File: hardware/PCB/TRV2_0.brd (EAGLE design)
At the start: 46 x 70 mm, 51 parts, among them IC1 TMP112, IC2 IC2, IC4 CNY70, IC5 ATMEGA8-AU, Q1 FC-12M, U1 DRV8850_RGY_24

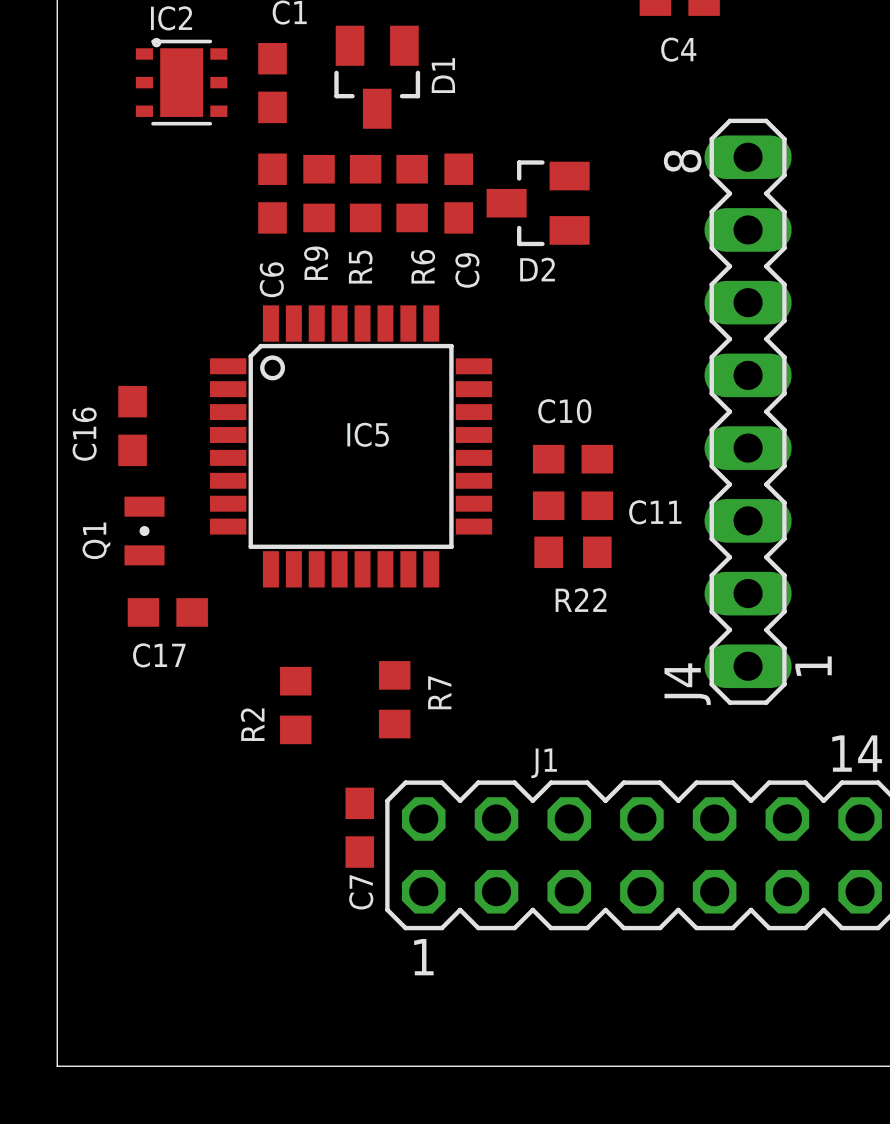
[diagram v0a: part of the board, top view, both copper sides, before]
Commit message: intial "core" tracks layed out
copy of tracks as per enlight
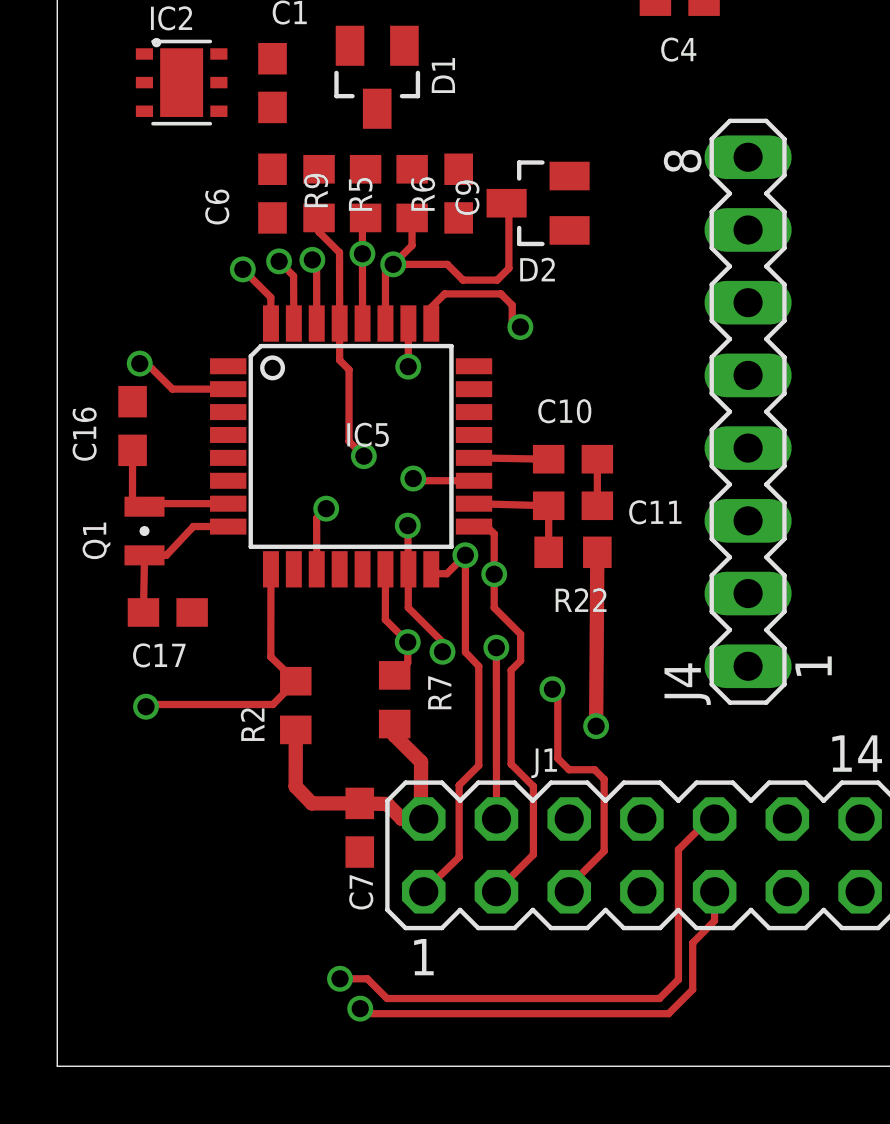
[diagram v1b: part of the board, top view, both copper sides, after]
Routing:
- net SDA: track 0.00 -> 29.5 mm, vias 0 -> 2
- net SCL: track 0.00 -> 19.5 mm, vias 0 -> 2
- net RESET: track 0.00 -> 17.8 mm, vias 0 -> 2
- net VCC: track 0.00 -> 16.7 mm, vias 0 -> 1
- net SPI_SCLK: track 0.00 -> 14.7 mm, vias 0 -> 1
- net SPI_MISO: track 0.00 -> 14.4 mm, vias 0 -> 1
- net SPI_MOSI: track 0.00 -> 10.9 mm, vias 0 -> 3
- net BUTTON_MODE_L: track 0.00 -> 9.88 mm, vias 0 -> 1
- net N$5: track 0.00 -> 5.35 mm
- net N$4: track 0.00 -> 5.23 mm
- net ML: track 0.00 -> 4.66 mm, vias 0 -> 1
- net AVCC: track 0.00 -> 4.23 mm
- net SPI_NNS: track 0.00 -> 4.22 mm, vias 0 -> 1
- net LED_HEATCALL_L: track 0.00 -> 3.46 mm, vias 0 -> 1
- net AREF: track 0.00 -> 2.61 mm
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
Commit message: Before routing tracks
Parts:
- moved J4 16.0 mm to (40.0, 21.0)
- moved C13 15.3 mm to (16.5, 47.0), turned to 180 degrees
- moved C12 12.3 mm to (16.5, 48.9), turned to 180 degrees
- moved C5 8.35 mm to (16.5, 45.1)
- moved J3 7.83 mm to (11.2, 52.6), turned to 180 degrees
- moved R3 7.24 mm to (10.8, 42.5), turned to 180 degrees
- moved R16 6.48 mm to (16.5, 43.2), turned to 180 degrees
- moved U1 1.80 mm to (11.4, 47.0)
- moved U$2 1.27 mm to (12.7, 70.5), flipped to the bottom
- turned R13 to 270 degrees
- turned VR1 to 270 degrees
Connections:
- net MC: now also IC5.22
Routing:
- net VCC: track 16.7 -> 210.5 mm, vias 1 -> 19
- net IO_POWER_UP: track 2.26 -> 124.3 mm, vias 1 -> 5
- net BUTTON_MODE_L: track 9.88 -> 89.9 mm, vias 1 -> 2
- net SDA: track 29.5 -> 91.0 mm, vias 2 -> 5
- net SCL: track 19.5 -> 80.5 mm, vias 2 -> 5
- net MI: track 2.15 -> 61.1 mm, vias 1 -> 6
- net DQ: track 2.30 -> 60.6 mm, vias 1 -> 2
- net TXD0: track 2.28 -> 56.3 mm, vias 1 -> 2
- net RXD0: track 2.38 -> 56.4 mm, vias 1 -> 2
- net LDR: track 0.00 -> 51.7 mm, vias 0 -> 4
- net POT: track 0.00 -> 49.6 mm, vias 0 -> 1
- net LED_HEATCALL_L: track 3.46 -> 52.0 mm, vias 1 -> 4
- net RFMIRQ: track 0.00 -> 45.5 mm, vias 0 -> 5
- net MR: track 1.51 -> 24.4 mm, vias 1 -> 2
- net SPI_SCLK: track 14.7 -> 35.7 mm, vias 1 -> 3
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- added copper zone on layer 1, net GND
- added copper zone on layer 16, net GND

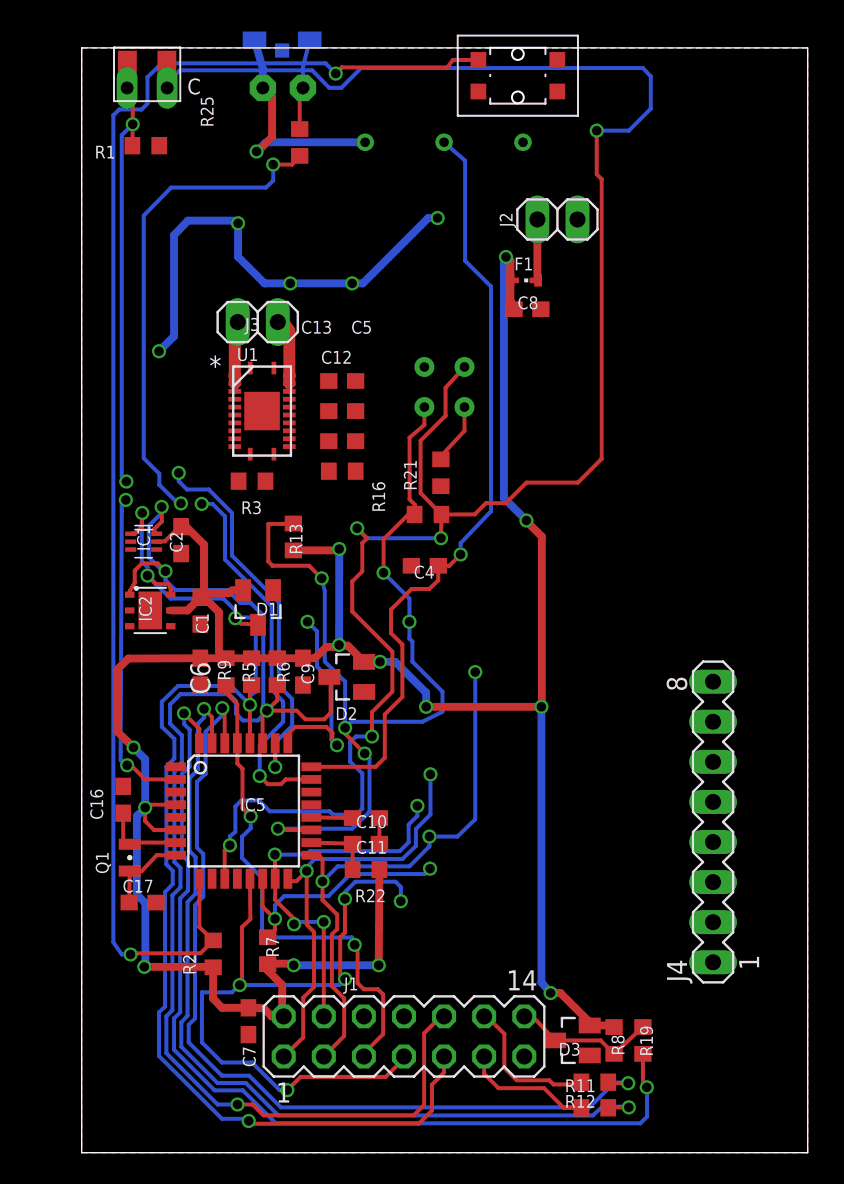
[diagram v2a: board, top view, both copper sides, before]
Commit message: 3 wires left
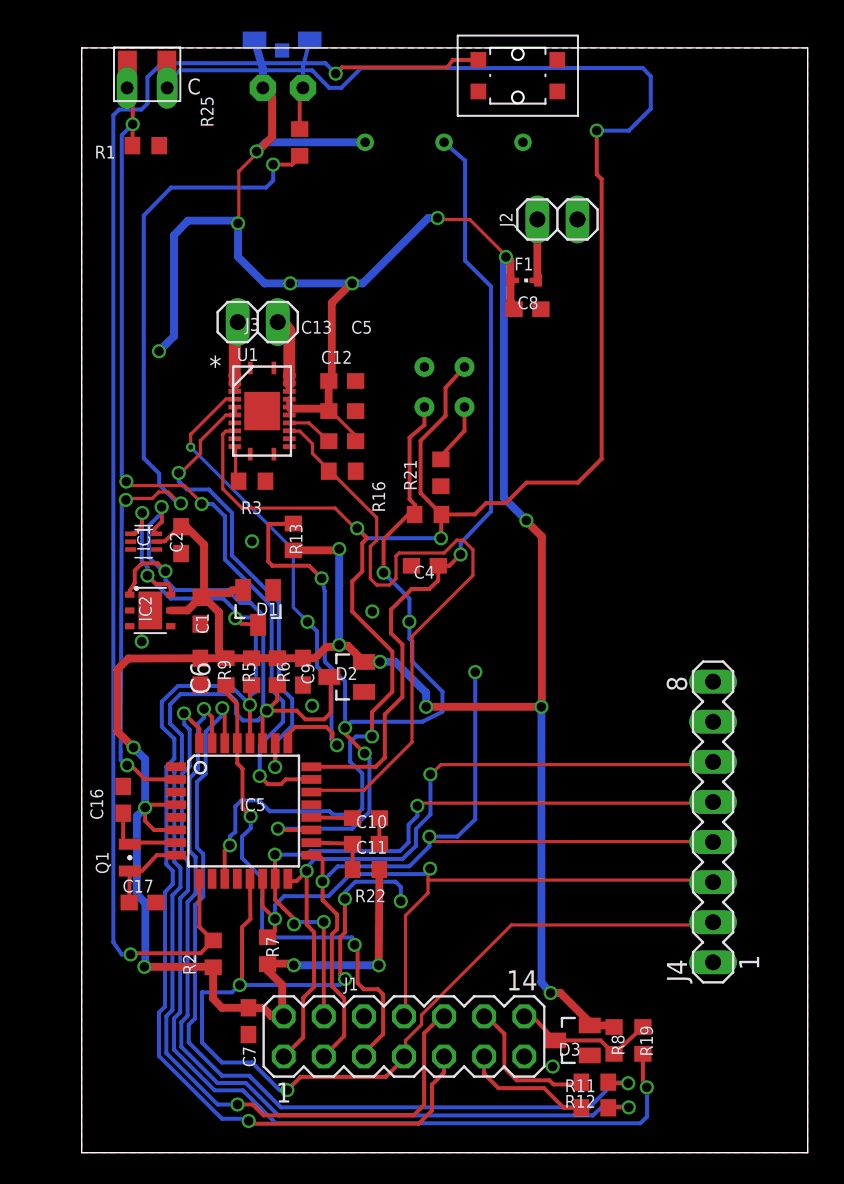
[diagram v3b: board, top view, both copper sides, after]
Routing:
- net MC: track 0.00 -> 42.7 mm
- net SPI_NNS: track 15.9 -> 44.0 mm
- net VCC: track 210.5 -> 236.0 mm
- net RFMIRQ: track 45.5 -> 69.6 mm
- net SPI_MOSI: track 24.2 -> 43.2 mm
- net ML: track 13.5 -> 32.4 mm, vias 2 -> 3
- net SPI_MISO: track 27.0 -> 45.2 mm
- net SPI_SCLK: track 35.7 -> 53.8 mm
- net IO_POWER_UP: track 124.3 -> 139.1 mm
- net MR: track 24.4 -> 30.5 mm
- net LDR: track 51.7 -> 57.1 mm
- net LED_HEATCALL_L: track 52.0 -> 56.0 mm
- net N$20: track 0.00 -> 2.95 mm
- net N$12: track 0.00 -> 2.32 mm
- net GND: vias 0 -> 5

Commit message: 2 wires left
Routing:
- net SPI_SCLK: track 53.8 -> 41.1 mm, vias 3 -> 2
- net GND: vias 5 -> 7
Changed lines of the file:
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@@
 <via x="3.81" y="32.385" extent="1-16" drill="0.6"/>
 <via x="10.795" y="38.735" extent="1-16" drill="0.6"/>
+<via x="25.4" y="32.385" extent="1-16" drill="0.6"/>
+<via x="17.78" y="28.067" extent="1-16" drill="0.6"/>
 <wire x1="6.2992" y1="37.9612" x2="4.75120625" y2="38.2176" width="0" layer="19" extent="1-1"/>
-<wire x1="17.8950125" y1="29.193196875" x2="14.605" y2="28.321" width="0" layer="19" extent="1-1"/>
 </signal>
 <signal name="SCL">
@@
 <wire x1="15.261809375" y1="16.012628125" x2="15.261809375" y2="17.184584375" width="0.254" layer="1"/>
 <via x="22.034925" y="20.030415625" extent="1-16" drill="0.6"/>
-<via x="24.93713125" y="30.4505125" extent="1-16" drill="0.6"/>
 <wire x1="22.034925" y1="20.030415625" x2="22.034925" y2="19.4093875" width="0.254" layer="16"/>
 <wire x1="22.034925" y1="19.4093875" x2="20.767975" y2="18.142434375" width="0.254" layer="16"/>
 <wire x1="20.767975" y1="18.142434375" x2="16.220103125" y2="18.142434375" width="0.254" layer="16"/>
 <wire x1="16.220103125" y1="18.142434375" x2="15.261809375" y2="17.184584375" width="0.254" layer="16"/>
-<wire x1="24.93713125" y1="30.4505125" x2="24.93713125" y2="21.12713125" width="0.254" layer="16"/>
-<wire x1="24.93713125" y1="21.12713125" x2="23.81013125" y2="20.030415625" width="0.254" layer="16"/>
-<wire x1="23.81013125" y1="20.030415625" x2="22.034925" y2="20.030415625" width="0.254" layer="16"/>
 <wire x1="22.352" y1="19.7104" x2="39.8272" y2="19.7104" width="0.2032" layer="1"/>
 <wire x1="22.1488" y1="19.9136" x2="22.352" y2="19.7104" width="0.2032" layer="1"/>

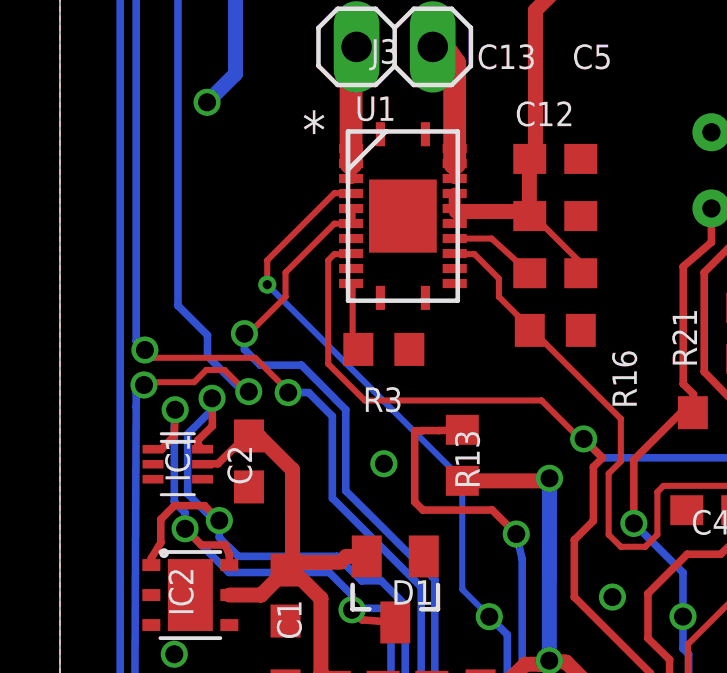
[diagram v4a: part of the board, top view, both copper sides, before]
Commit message: all wires done - need to do ERC and DRC
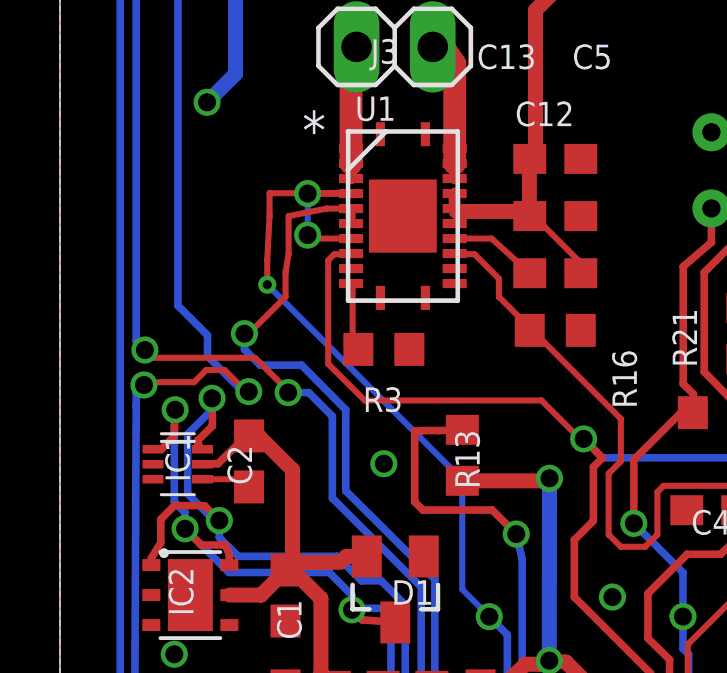
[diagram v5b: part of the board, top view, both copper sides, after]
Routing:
- net ML: track 32.4 -> 38.0 mm, vias 3 -> 5
- net GND: track 1.63 -> 3.43 mm
- net MR: track 30.5 -> 31.8 mm
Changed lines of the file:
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@@
 <via x="25.4" y="32.385" extent="1-16" drill="0.6"/>
 <via x="17.78" y="28.067" extent="1-16" drill="0.6"/>
-<wire x1="6.2992" y1="37.9612" x2="4.75120625" y2="38.2176" width="0" layer="19" extent="1-1"/>
+<wire x1="4.75120625" y1="38.2176" x2="6.2992" y2="38.2176" width="0.2032" layer="1"/>
+<wire x1="6.2992" y1="38.2176" x2="6.2992" y2="37.9612" width="0.4064" layer="1"/>
 </signal>
 <signal name="SCL">
@@
 <wire x1="16.174684375" y1="25.825634375" x2="16.174684375" y2="25.81956875" width="0.254" layer="16"/>
 <wire x1="9.7026" y1="47.74" x2="9.41" y2="47.74" width="0.254" layer="1"/>
-<wire x1="9.144" y1="47.752" x2="9.3472" y2="47.752" width="0.2032" layer="1"/>
-<wire x1="6.9088" y1="45.5168" x2="9.144" y2="47.752" width="0.2032" layer="1"/>
+<wire x1="6.9088" y1="45.5168" x2="6.985" y2="46.99" width="0.2032" layer="1"/>
+<wire x1="6.985" y1="46.99" x2="6.985" y2="47.752" width="0.2032" layer="1"/>
+<wire x1="6.985" y1="47.752" x2="9.3472" y2="47.752" width="0.2032" layer="1"/>
 <wire x1="6.9088" y1="44.704" x2="6.9088" y2="45.5168" width="0.2032" layer="1"/>
 <wire x1="13.4112" y1="38.2016" x2="6.9088" y2="44.704" width="0.2032" layer="16"/>
@@
 <wire x1="14.4272" y1="33.7312" x2="14.310025" y2="33.636434375" width="0.2032" layer="16"/>
 <via x="6.9088" y="44.704" extent="1-16" drill="0.3048"/>
-<wire x1="9.7026" y1="47.74" x2="9.7026" y2="46.24" width="0" layer="19" extent="1-1"/>
+<wire x1="9.7026" y1="46.24" x2="8.37" y2="46.24" width="0.2032" layer="1"/>
+<wire x1="9.7026" y1="47.74" x2="8.255" y2="47.74" width="0.2032" layer="1"/>
+<wire x1="8.255" y1="47.74" x2="8.255" y2="46.355" width="0.2032" layer="16"/>
+<via x="8.255" y="47.74" extent="1-16" drill="0.6"/>
+<via x="8.255" y="46.355" extent="1-16" drill="0.6"/>
+<wire x1="8.37" y1="46.24" x2="8.255" y2="46.355" width="0.2032" layer="1"/>
 </signal>
 <signal name="MR">
@@
 <wire x1="9.7536" y1="46.736" x2="9.7026" y2="46.74" width="0.2032" layer="1"/>
 <wire x1="9.7536" y1="47.1424" x2="9.7026" y2="47.24" width="0.2032" layer="1"/>
-<wire x1="9.144" y1="46.736" x2="9.5504" y2="46.736" width="0.2032" layer="1"/>
-<wire x1="7.5184" y1="45.1104" x2="9.144" y2="46.736" width="0.2032" layer="1"/>
+<wire x1="7.5184" y1="45.1104" x2="7.62" y2="45.72" width="0.2032" layer="1"/>
+<wire x1="7.62" y1="45.72" x2="7.62" y2="46.99" width="0.2032" layer="1"/>
 <wire x1="7.5184" y1="44.2976" x2="7.5184" y2="45.1104" width="0.2032" layer="1"/>
 <wire x1="6.2992" y1="43.0784" x2="7.5184" y2="44.2976" width="0.2032" layer="1"/>
 <wire x1="9.5504" y1="46.736" x2="9.7026" y2="46.74" width="0.2032" layer="1"/>
 <wire x1="6.2992" y1="43.0784" x2="6.1479875" y2="43.0694875" width="0.2032" layer="1"/>
+<wire x1="7.62" y1="46.99" x2="8.89" y2="47.24" width="0.2032" layer="1"/>
+<wire x1="8.89" y1="47.24" x2="9.7026" y2="47.24" width="0.2032" layer="1"/>
 </signal>
 </signals>

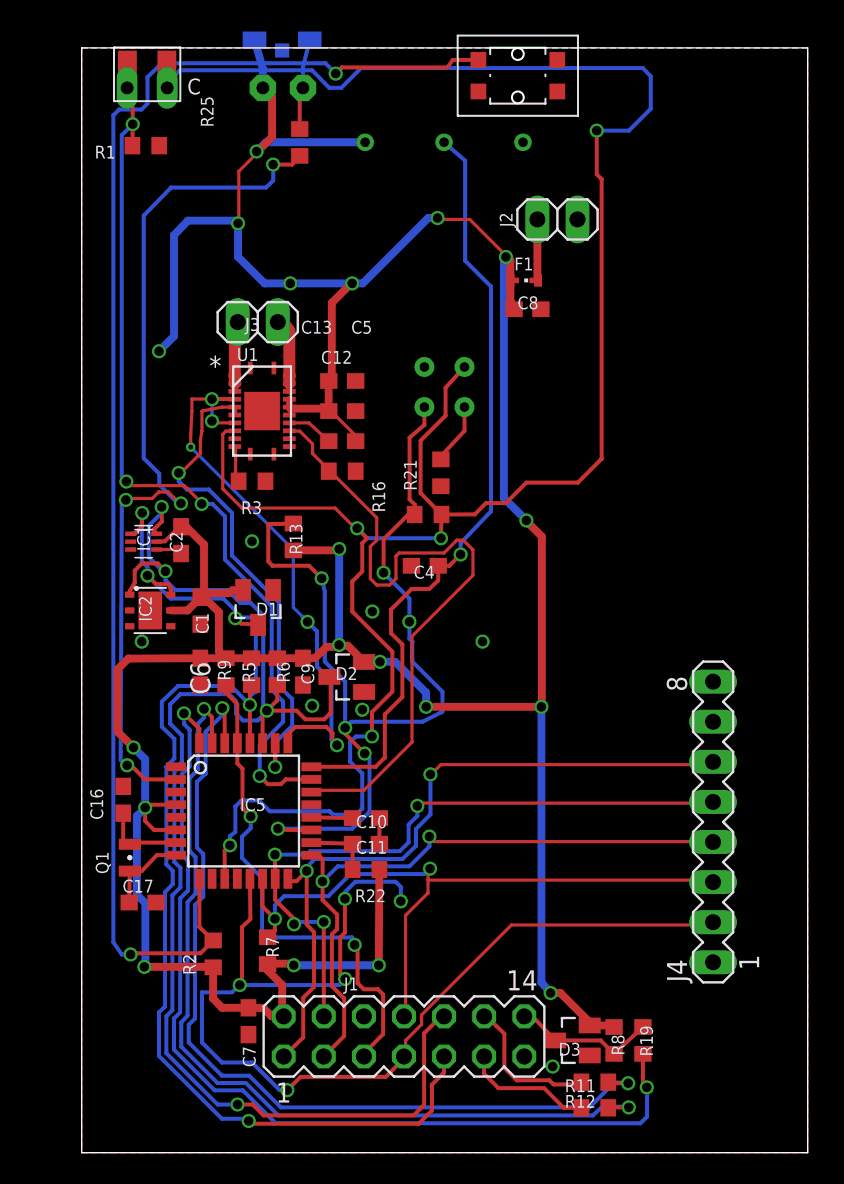
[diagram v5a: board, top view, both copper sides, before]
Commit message: DRV8850 lbr added and a whole BIG lot of DRC's sorted
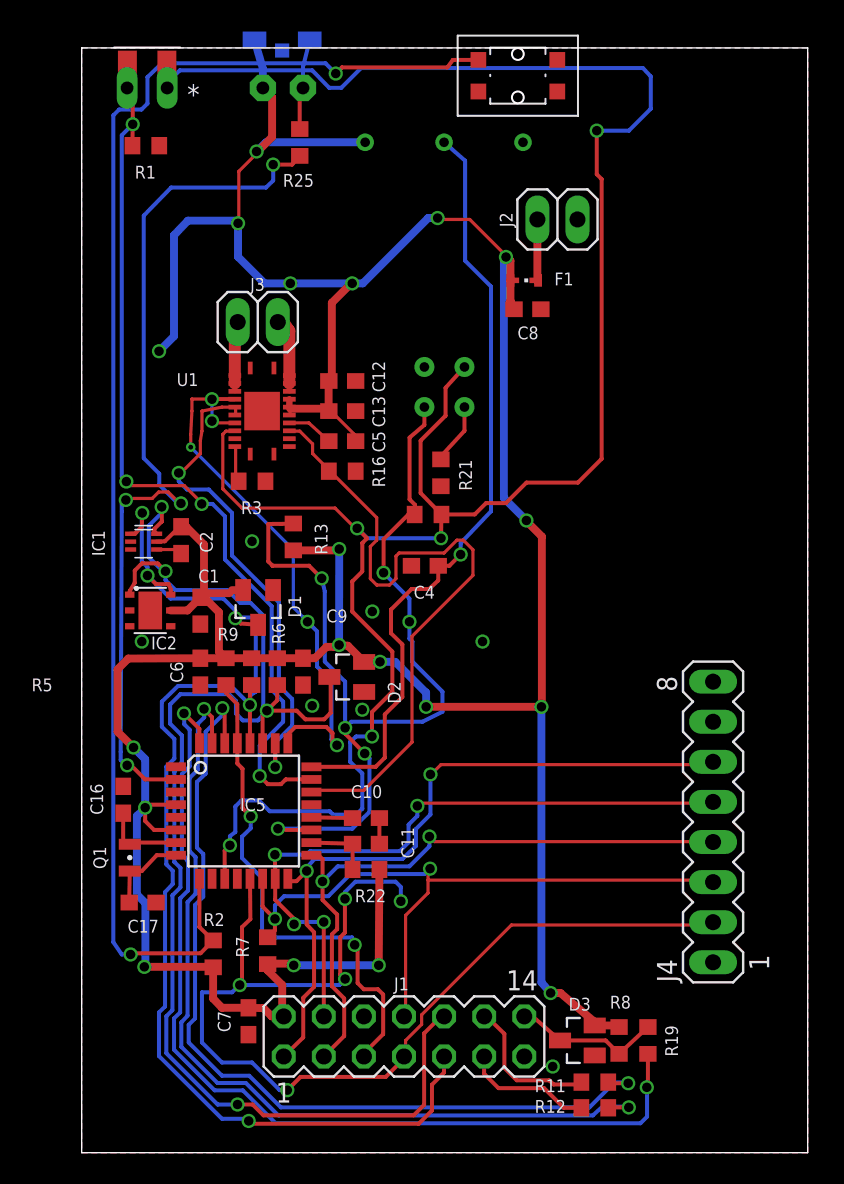
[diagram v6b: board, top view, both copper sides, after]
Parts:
- moved D3 0.32 mm to (31.4, 7.11)
- moved R19 0.32 mm to (35.9, 7.11)
- moved R8 0.32 mm to (34.0, 7.11)

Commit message: near done :-D
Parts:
- moved R1 1.31 mm to (5.33, 63.5)
- moved U$1 0.13 mm to (4.15, 68.2)
- renumbered Q1 to X1
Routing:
- net SCL: track 80.6 -> 82.3 mm
- net ML: track 38.0 -> 39.6 mm
- net MR: track 31.8 -> 32.3 mm
- net RFMIRQ: track 69.6 -> 69.1 mm
- net SDA: track 91.0 -> 91.4 mm, vias 5 -> 4
